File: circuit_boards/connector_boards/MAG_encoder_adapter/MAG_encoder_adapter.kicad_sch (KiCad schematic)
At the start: 5 parts, among them J1 Mag-encoder, J2 POT, J3 RIO

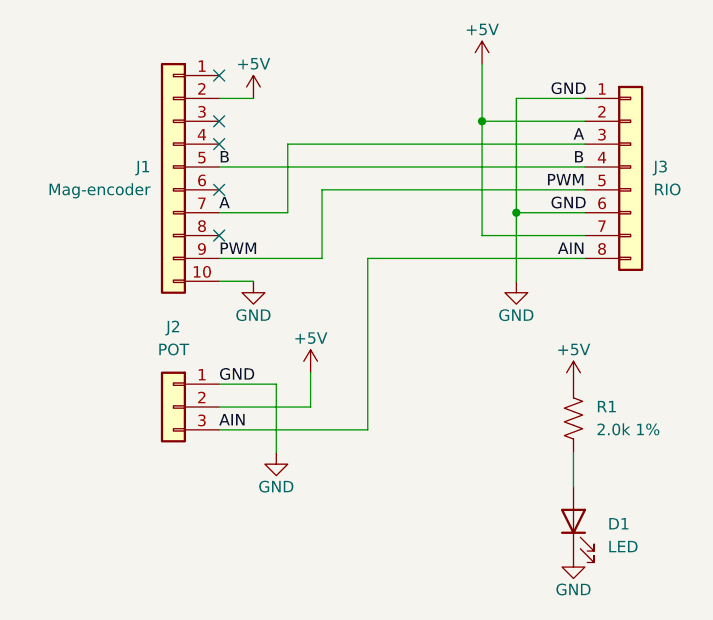
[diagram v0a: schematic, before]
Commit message: Fix mag encoder board
Signed-off-by: Henry Speiser <henry@speiser.net>
Change-Id: Ibd00abfba0a6230b25acf3f77c01d51ace0d4a3c
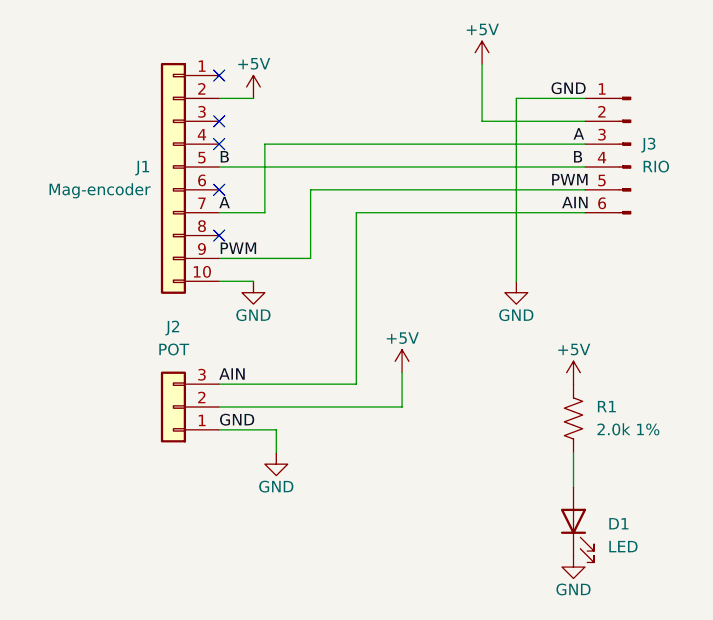
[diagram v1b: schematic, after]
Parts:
- removed J3: RIO, MAG-encoder:0705550007, symbol Connector_Generic:Conn_01x08
- added J3: RIO, mag:705550005, symbol Connector:Conn_01x06_Male
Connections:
- net +5V: now also J3.2 (Pin_2)
- net A: now also J3.3 (Pin_3)
- net AIN: now also J3.6 (Pin_6)
- net B: now also J3.4 (Pin_4)
- net GND: now also J3.1 (Pin_1)
- net PWM: now also J3.5 (Pin_5)
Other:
- moved on the sheet: J2
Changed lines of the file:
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@@
     (company "971 Spartan Robotics")
-  )
-  (junction (at 146.05 87.63) (diameter 0) (color 0 0 0 0)
-  )
-  (junction (at 149.86 97.79) (diameter 0) (color 0 0 0 0)
   )
   (no_connect (at 116.84 100.33))
@@
   (no_connect (at 116.84 82.55))
   (no_connect (at 116.84 95.25))
-  (wire (pts (xy 127 119.38) (xy 127 115.57))
-    (stroke (width 0) (type default) (color 0 0 0 0))
-  )
-  (wire (pts (xy 123.19 116.84) (xy 123.19 124.46))
+  (wire (pts (xy 149.86 85.09) (xy 157.48 85.09))
+    (stroke (width 0) (type default) (color 0 0 0 0))
+  )
+  (wire (pts (xy 116.84 92.71) (xy 157.48 92.71))
+    (stroke (width 0) (type default) (color 0 0 0 0))
+  )
+  (wire (pts (xy 121.92 90.17) (xy 121.92 97.79))
     (stroke (width 0) (type default) (color 0 0 0 0))
   )
@@
     (stroke (width 0) (type default) (color 0 0 0 0))
   )
-  (wire (pts (xy 146.05 87.63) (xy 157.48 87.63))
+  (wire (pts (xy 157.48 97.79) (xy 132.08 97.79))
     (stroke (width 0) (type default) (color 0 0 0 0))
   )
@@
     (stroke (width 0) (type default) (color 0 0 0 0))
   )
-  (wire (pts (xy 149.86 97.79) (xy 157.48 97.79))
-    (stroke (width 0) (type default) (color 0 0 0 0))
-  )
-  (wire (pts (xy 124.46 97.79) (xy 124.46 90.17))
-    (stroke (width 0) (type default) (color 0 0 0 0))
-  )
-  (wire (pts (xy 146.05 100.33) (xy 157.48 100.33))
-    (stroke (width 0) (type default) (color 0 0 0 0))
-  )
-  (wire (pts (xy 116.84 102.87) (xy 128.27 102.87))
+  (wire (pts (xy 116.84 97.79) (xy 121.92 97.79))
+    (stroke (width 0) (type default) (color 0 0 0 0))
+  )
+  (wire (pts (xy 127 95.25) (xy 127 102.87))
+    (stroke (width 0) (type default) (color 0 0 0 0))
+  )
+  (wire (pts (xy 149.86 105.41) (xy 149.86 85.09))
     (stroke (width 0) (type default) (color 0 0 0 0))
   )
@@
     (stroke (width 0) (type default) (color 0 0 0 0))
   )
-  (wire (pts (xy 146.05 81.28) (xy 146.05 87.63))
-    (stroke (width 0) (type default) (color 0 0 0 0))
-  )
-  (wire (pts (xy 133.35 121.92) (xy 133.35 102.87))
-    (stroke (width 0) (type default) (color 0 0 0 0))
-  )
-  (wire (pts (xy 116.84 121.92) (xy 133.35 121.92))
-    (stroke (width 0) (type default) (color 0 0 0 0))
-  )
-  (wire (pts (xy 128.27 102.87) (xy 128.27 95.25))
-    (stroke (width 0) (type default) (color 0 0 0 0))
-  )
-  (wire (pts (xy 124.46 90.17) (xy 157.48 90.17))
-    (stroke (width 0) (type default) (color 0 0 0 0))
-  )
-  (wire (pts (xy 149.86 85.09) (xy 157.48 85.09))
-    (stroke (width 0) (type default) (color 0 0 0 0))
-  )
-  (wire (pts (xy 128.27 95.25) (xy 157.48 95.25))
-    (stroke (width 0) (type default) (color 0 0 0 0))
-  )
-  (wire (pts (xy 116.84 116.84) (xy 123.19 116.84))
-    (stroke (width 0) (type default) (color 0 0 0 0))
-  )
-  (wire (pts (xy 116.84 119.38) (xy 127 119.38))
-    (stroke (width 0) (type default) (color 0 0 0 0))
-  )
-  (wire (pts (xy 149.86 97.79) (xy 149.86 105.41))
-    (stroke (width 0) (type default) (color 0 0 0 0))
-  )
-  (wire (pts (xy 116.84 97.79) (xy 124.46 97.79))
-    (stroke (width 0) (type default) (color 0 0 0 0))
-  )
-  (wire (pts (xy 133.35 102.87) (xy 157.48 102.87))
-    (stroke (width 0) (type default) (color 0 0 0 0))
-  )
-  (wire (pts (xy 116.84 92.71) (xy 157.48 92.71))
-    (stroke (width 0) (type default) (color 0 0 0 0))
-  )
-  (wire (pts (xy 146.05 100.33) (xy 146.05 87.63))
-    (stroke (width 0) (type default) (color 0 0 0 0))
-  )
-  (wire (pts (xy 149.86 85.09) (xy 149.86 97.79))
-    (stroke (width 0) (type default) (color 0 0 0 0))
-  )
-  (label "B" (at 156.21 92.71 0)
+  (wire (pts (xy 127 102.87) (xy 116.84 102.87))
+    (stroke (width 0) (type default) (color 0 0 0 0))
+  )
+  (wire (pts (xy 137.16 119.38) (xy 137.16 115.57))
+    (stroke (width 0) (type default) (color 0 0 0 0))
+  )
+  (wire (pts (xy 146.05 87.63) (xy 146.05 81.28))
+    (stroke (width 0) (type default) (color 0 0 0 0))
+  )
+  (wire (pts (xy 132.08 97.79) (xy 132.08 116.84))
+    (stroke (width 0) (type default) (color 0 0 0 0))
+  )
+  (wire (pts (xy 116.84 116.84) (xy 132.08 116.84))
+    (stroke (width 0) (type default) (color 0 0 0 0))
+  )
+  (wire (pts (xy 116.84 119.38) (xy 137.16 119.38))
+    (stroke (width 0) (type default) (color 0 0 0 0))
+  )
+  (wire (pts (xy 157.48 87.63) (xy 146.05 87.63))
+    (stroke (width 0) (type default) (color 0 0 0 0))
+  )
+  (wire (pts (xy 121.92 90.17) (xy 157.48 90.17))
+    (stroke (width 0) (type default) (color 0 0 0 0))
+  )
+  (wire (pts (xy 127 95.25) (xy 157.48 95.25))
+    (stroke (width 0) (type default) (color 0 0 0 0))
+  )
+  (wire (pts (xy 123.19 124.46) (xy 123.19 121.92))
+    (stroke (width 0) (type default) (color 0 0 0 0))
+  )
+  (wire (pts (xy 116.84 121.92) (xy 123.19 121.92))
+    (stroke (width 0) (type default) (color 0 0 0 0))
+  )
+  (label "AIN" (at 116.84 116.84 0)
+    (effects (font (size 1.27 1.27)) (justify left bottom))
+  )
+  (label "B" (at 156.0934 92.71 0)
     (effects (font (size 1.27 1.27)) (justify left bottom))
   )
@@
     (effects (font (size 1.27 1.27)) (justify left bottom))
   )
-  (label "GND" (at 116.84 116.84 0)
-    (effects (font (size 1.27 1.27)) (justify left bottom))
-  )
-  (label "AIN" (at 116.84 121.92 0)
-    (effects (font (size 1.27 1.27)) (justify left bottom))
-  )
   (label "GND" (at 153.67 85.09 0)
     (effects (font (size 1.27 1.27)) (justify left bottom))
@@
     (effects (font (size 1.27 1.27)) (justify left bottom))
   )
+  (label "GND" (at 116.84 121.92 0)
+    (effects (font (size 1.27 1.27)) (justify left bottom))
+  )
+  (label "AIN" (at 154.94 97.79 0)
+    (effects (font (size 1.27 1.27)) (justify left bottom))
+  )
+  (label "PWM" (at 153.67 95.25 0)
+    (effects (font (size 1.27 1.27)) (justify left bottom))
+  )
   (label "A" (at 156.21 90.17 0)
     (effects (font (size 1.27 1.27)) (justify left bottom))
   )
-  (label "AIN" (at 157.48 102.87 180)
-    (effects (font (size 1.27 1.27)) (justify right bottom))
-  )
-  (label "GND" (at 153.67 97.79 0)
-    (effects (font (size 1.27 1.27)) (justify left bottom))
-  )
-  (label "PWM" (at 157.48 95.25 180)
-    (effects (font (size 1.27 1.27)) (justify right bottom))
+  (symbol (lib_id "Connector:Conn_01x06_Male") (at 162.56 90.17 0) (mirror y) (unit 1)
+    (in_bom yes) (on_board yes) (fields_autoplaced)
+    (property "Reference" "J3" (id 0) (at 163.83 90.1699 0)
+      (effects (font (size 1.27 1.27)) (justify right))
+    )
+    (property "Value" "RIO" (id 1) (at 163.83 92.7099 0)
+      (effects (font (size 1.27 1.27)) (justify right))
+    )
+    (property "Footprint" "mag:705550005" (id 2) (at 162.56 90.17 0)
+      (effects (font (size 1.27 1.27)) hide)
+    )
+    (property "Datasheet" "~" (id 3) (at 162.56 90.17 0)
+      (effects (font (size 1.27 1.27)) hide)
+    )
+    (pin "1")
+    (pin "2")
+    (pin "3")
+    (pin "4")
+    (pin "5")
+    (pin "6")
   )
   (symbol (lib_id "Device:R_US") (at 156.21 120.65 180) (unit 1)
@@
     (pin "2")
   )
-  (symbol (lib_id "Connector_Generic:Conn_01x08") (at 162.56 92.71 0) (unit 1)
-    (in_bom yes) (on_board yes) (fields_autoplaced)
-    (property "Reference" "J3" (id 0) (at 165.1 92.7099 0)
-      (effects (font (size 1.27 1.27)) (justify left))
-    )
-    (property "Value" "RIO" (id 1) (at 165.1 95.2499 0)
-      (effects (font (size 1.27 1.27)) (justify left))
-    )
-    (property "Footprint" "MAG-encoder:0705550007" (id 2) (at 162.56 92.71 0)
-      (effects (font (size 1.27 1.27)) hide)
-    )
-    (property "Datasheet" "~" (id 3) (at 162.56 92.71 0)
-      (effects (font (size 1.27 1.27)) hide)
-    )
-    (property "MFG P/N" "0705550007" (id 4) (at 162.56 92.71 0)
-      (effects (font (size 1.27 1.27)) hide)
-    )
-    (property "MFG" "MOLEX" (id 5) (at 162.56 92.71 0)
-      (effects (font (size 1.27 1.27)) hide)
-    )
-    (pin "1")
-    (pin "2")
-    (pin "3")
-    (pin "4")
-    (pin "5")
-    (pin "6")
-    (pin "7")
-    (pin "8")
-  )
   (symbol (lib_id "power:GND") (at 149.86 105.41 0) (unit 1)
     (in_bom yes) (on_board yes)
@@
     (pin "1")
   )
-  (symbol (lib_id "Connector_Generic:Conn_01x03") (at 111.76 119.38 0) (mirror y) (unit 1)
+  (symbol (lib_id "Connector_Generic:Conn_01x03") (at 111.76 119.38 180) (unit 1)
     (in_bom yes) (on_board yes) (fields_autoplaced)
     (property "Reference" "J2" (id 0) (at 111.76 110.49 0))
@@
     (pin "3")
   )
-  (symbol (lib_id "power:+5V") (at 127 115.57 0) (unit 1)
-    (in_bom yes) (on_board yes)
-    (property "Reference" "#PWR04" (id 0) (at 127 119.38 0)
-      (effects (font (size 1.27 1.27)) hide)
-    )
-    (property "Value" "+5V" (id 1) (at 127 111.76 0))
-    (property "Footprint" "" (id 2) (at 127 115.57 0)
-      (effects (font (size 1.27 1.27)) hide)
-    )
-    (property "Datasheet" "" (id 3) (at 127 115.57 0)
+  (symbol (lib_id "power:+5V") (at 137.16 115.57 0) (unit 1)
+    (in_bom yes) (on_board yes)
+    (property "Reference" "#PWR04" (id 0) (at 137.16 119.38 0)
+      (effects (font (size 1.27 1.27)) hide)
+    )
+    (property "Value" "+5V" (id 1) (at 137.16 111.76 0))
+    (property "Footprint" "" (id 2) (at 137.16 115.57 0)
+      (effects (font (size 1.27 1.27)) hide)
+    )
+    (property "Datasheet" "" (id 3) (at 137.16 115.57 0)
       (effects (font (size 1.27 1.27)) hide)
     )
@@
       (reference "J2") (unit 1) (value "POT") (footprint "MAG-encoder:70555-0002")
     )
-    (path "/611e208d-2626-4f2a-9fb5-7f790284a4fe"
-      (reference "J3") (unit 1) (value "RIO") (footprint "MAG-encoder:0705550007")
+    (path "/014e8c36-32b1-4c25-92d8-67829df95144"
+      (reference "J3") (unit 1) (value "RIO") (footprint "mag:705550005")
     )
     (path "/01b86c7a-bf18-4712-ae4d-dc895521505c"
